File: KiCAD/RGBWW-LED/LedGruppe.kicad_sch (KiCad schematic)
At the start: 12 parts, among them U1 H5050RGBWW-ZB-96427, U2 H5050RGBWW-ZB-96427, U3 WS2805, U4 H5050RGBWW-ZB-96427

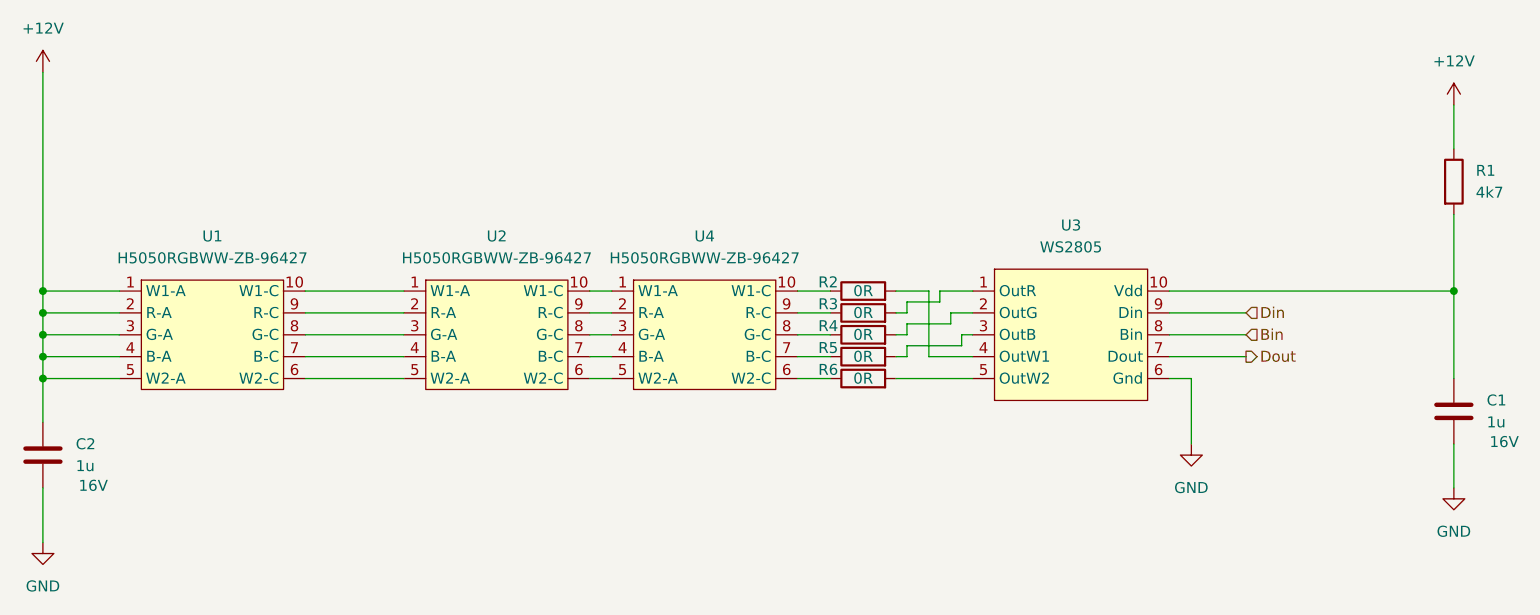
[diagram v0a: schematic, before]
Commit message: added some library components and edited pdf
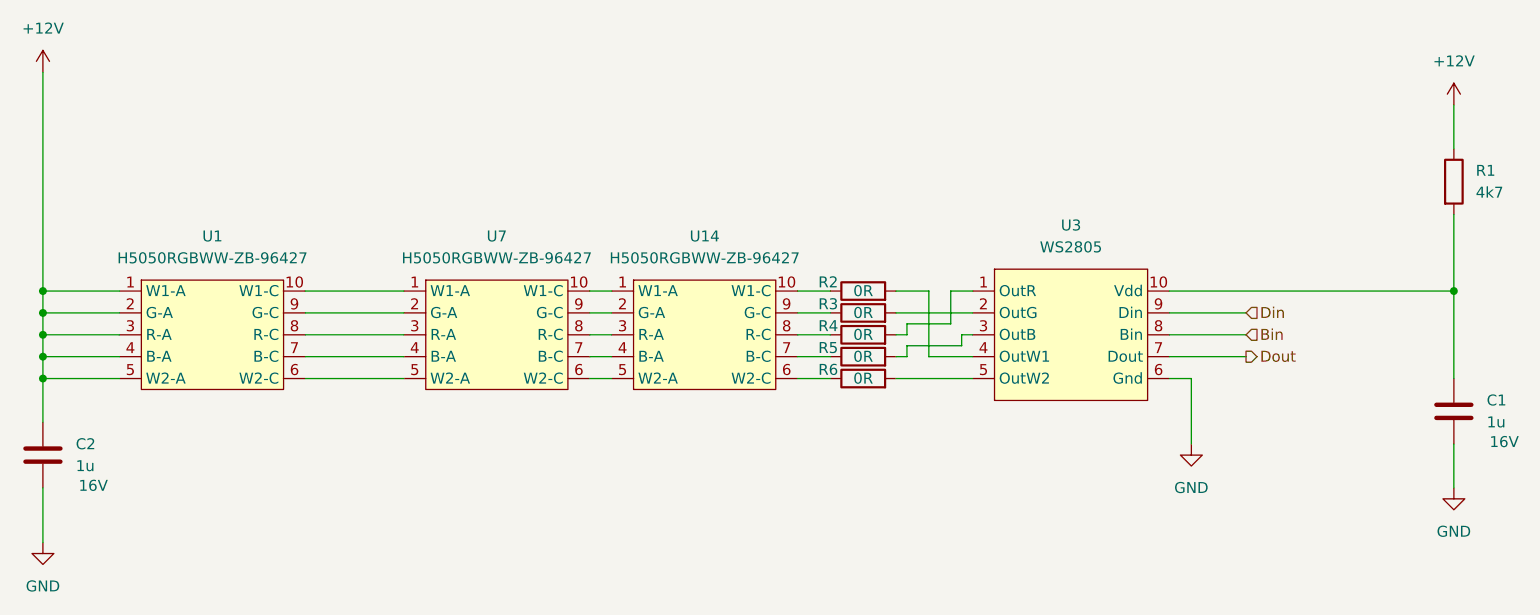
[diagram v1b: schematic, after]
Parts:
- removed U1, U2, U4: H5050RGBWW-ZB-96427, symbol RGBWW-LED-ProjectLib:H5050RGBWW-ZB-96427
- added U1, U14, U7: H5050RGBWW-ZB-96427, LEDandDriver:LED_RGBWW_5050_10, symbol RGBWWlIBS:H5050RGBWW-ZB-96427
- U3: footprint (none) -> LEDandDriver:SOP-10-6mm-1mm
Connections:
- net +12V: now also U1.1 (W1-A), U1.2 (G-A), U1.3 (R-A), U1.4 (B-A), U1.5 (W2-A)
- net at R6.1: now also U14.6 (W2-C)
- net at R4.1: now also U14.8 (R-C)
- net at R4.2: now also U3.1 (OutR); no longer U3.2 (OutG)
- net at R3.2: now also U3.2 (OutG); no longer U3.1 (OutR)
- net at R5.1: now also U14.7 (B-C)
- net at R2.1: now also U14.10 (W1-C)
- net at R3.1: now also U14.9 (G-C)
- new net: U1.10 (W1-C), U7.1 (W1-A)
- new net: U14.1 (W1-A), U7.10 (W1-C)
- new net: U1.9 (G-C), U7.2 (G-A)
- new net: U1.8 (R-C), U7.3 (R-A)
- new net: U1.7 (B-C), U7.4 (B-A)
- new net: U1.6 (W2-C), U7.5 (W2-A)
- new net: U14.5 (W2-A), U7.6 (W2-C)
- new net: U14.4 (B-A), U7.7 (B-C)
- new net: U14.3 (R-A), U7.8 (R-C)
- new net: U14.2 (G-A), U7.9 (G-C)

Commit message: started layout, some mods to the lib
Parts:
- R2, R3, R4, R5, R6: value 0R -> 10R
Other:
- moved on the sheet: U7
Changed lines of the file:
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@@
 	(wire
 		(pts
-			(xy 106.68 96.52) (xy 104.14 96.52)
+			(xy 106.68 96.52) (xy 100.33 96.52)
 		)
 		(stroke
@@
 	(wire
 		(pts
-			(xy 82.55 88.9) (xy 71.12 88.9)
+			(xy 78.74 88.9) (xy 71.12 88.9)
 		)
 		(stroke
@@
 	(wire
 		(pts
-			(xy 82.55 91.44) (xy 71.12 91.44)
+			(xy 78.74 91.44) (xy 71.12 91.44)
 		)
 		(stroke
@@
 	(wire
 		(pts
-			(xy 106.68 99.06) (xy 104.14 99.06)
+			(xy 106.68 99.06) (xy 100.33 99.06)
 		)
 		(stroke
@@
 	(wire
 		(pts
-			(xy 82.55 93.98) (xy 71.12 93.98)
+			(xy 78.74 93.98) (xy 71.12 93.98)
 		)
 		(stroke
@@
 	(wire
 		(pts
-			(xy 82.55 99.06) (xy 71.12 99.06)
+			(xy 78.74 99.06) (xy 71.12 99.06)
 		)
 		(stroke
@@
 	(wire
 		(pts
-			(xy 106.68 91.44) (xy 104.14 91.44)
+			(xy 106.68 91.44) (xy 100.33 91.44)
 		)
 		(stroke
@@
 	(wire
 		(pts
-			(xy 82.55 96.52) (xy 71.12 96.52)
+			(xy 78.74 96.52) (xy 71.12 96.52)
 		)
 		(stroke
@@
 	(wire
 		(pts
-			(xy 106.68 88.9) (xy 104.14 88.9)
-		)
-		(stroke
-			(width 0)
-			(type default)
-		)
-	)
-	(wire
-		(pts
-			(xy 106.68 93.98) (xy 104.14 93.98)
+			(xy 106.68 88.9) (xy 100.33 88.9)
+		)
+		(stroke
+			(width 0)
+			(type default)
+		)
+	)
+	(wire
+		(pts
+			(xy 106.68 93.98) (xy 100.33 93.98)
 		)
 		(stroke
@@
 			)
 		)
-		(property "Value" "0R"
+		(property "Value" "10R"
 			(at 135.89 99.06 90)
 			(show_name no)
@@
 			)
 		)
-		(property "Value" "0R"
+		(property "Value" "10R"
 			(at 135.89 93.98 90)
 			(show_name no)
@@
 	(symbol
 		(lib_id "RGBWWlIBS:H5050RGBWW-ZB-96427")
-		(at 93.98 86.36 0)
+		(at 90.17 86.36 0)
 		(unit 1)
 		(body_style 1)
@@
 		(fields_autoplaced yes)
 		(property "Reference" "U7"
-			(at 93.345 82.55 0)
+			(at 89.535 82.55 0)
 			(show_name no)
 			(do_not_autoplace no)
@@
 		)
 		(property "Value" "H5050RGBWW-ZB-96427"
-			(at 93.345 85.09 0)
+			(at 89.535 85.09 0)
 			(show_name no)
 			(do_not_autoplace no)
@@
 		)
 		(property "Footprint" "LEDandDriver:LED_RGBWW_5050_10"
-			(at 93.98 86.36 0)
+			(at 90.17 86.36 0)
 			(hide yes)
 			(show_name no)
@@
 		)
 		(property "Datasheet" ""
-			(at 93.98 86.36 0)
+			(at 90.17 86.36 0)
 			(hide yes)
 			(show_name no)
@@
 		)
 		(property "Description" ""
-			(at 93.98 86.36 0)
+			(at 90.17 86.36 0)
 			(hide yes)
 			(show_name no)
@@
 			)
 		)
-		(property "Value" "0R"
+		(property "Value" "10R"
 			(at 135.89 96.52 90)
 			(show_name no)
@@
 			)
 		)
-		(property "Value" "0R"
+		(property "Value" "10R"
 			(at 135.89 88.9 90)
 			(show_name no)
@@
 			)
 		)
-		(property "Value" "0R"
+		(property "Value" "10R"
 			(at 135.89 91.44 90)
 			(show_name no)

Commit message: added some datasheet and started controller
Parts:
- C1, C2: footprint Capacitor_SMD:C_0603_1608Metric -> LEDandDriver:C_0603_1608Metric_LedPrj
- R1, R2, R3, R4, R5, R6: footprint Resistor_SMD:R_0603_1608Metric -> LEDandDriver:R_0603_1608Metric_LedPrj
- U3: footprint LEDandDriver:SOP-10-6mm-1mm -> Package_SO:SOIC-10_3.9x4.9mm_P1mm
